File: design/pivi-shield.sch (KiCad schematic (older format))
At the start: 3 parts

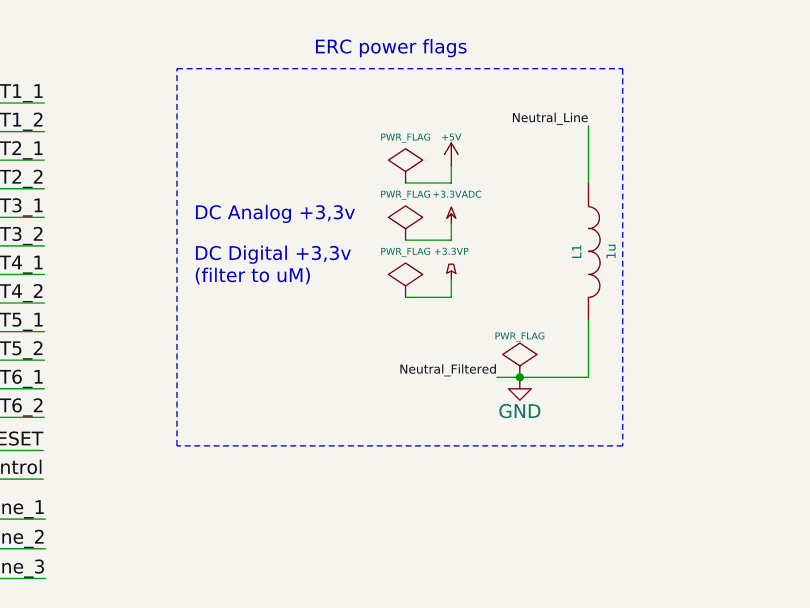
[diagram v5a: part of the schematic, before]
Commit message: Fix #10: main route not connected.
Right now we have the following power labels:
* +5V from 220v to Raspberry pi and voltage regulator.
* +3V3 from voltage regulator to microcontroller imput and measurement voltage circuit.
* +3.3VP DC digital +3.3v (filter to MCU).
* +3.3VADC DC analog +3.3v
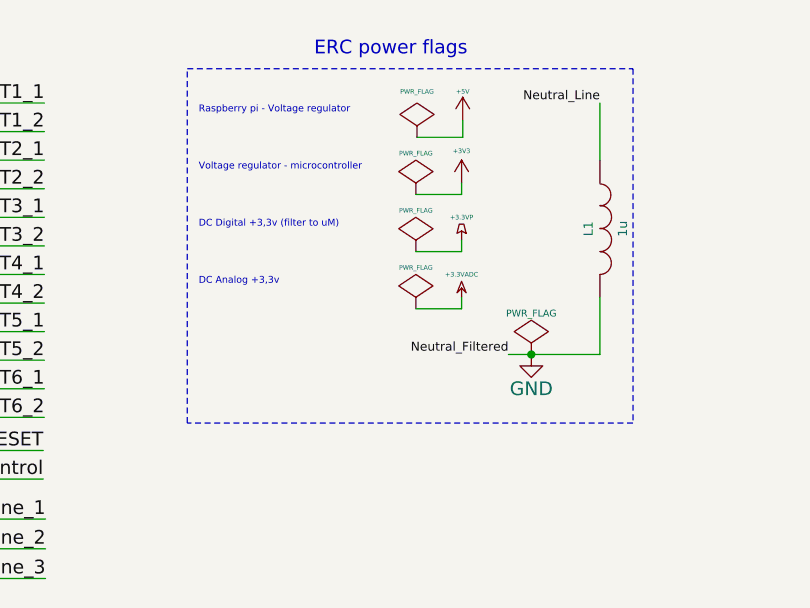
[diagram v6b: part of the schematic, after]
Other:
- note added: "DC Digital +3,3v (filter to uM)"
- note added: "Raspberry pi - Voltage regulator"
- note added: "Voltage regulator - microcontroller"
- note removed: "DC Digital +3,3v\n(filter to uM)"
- moved on the sheet: L1
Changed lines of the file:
@@
 LIBS:txs0104e
 LIBS:less
-LIBS:pivi-shield-cache
 EELAYER 25 0
 EELAYER END
@@
 L +5V #PWR01
 U 1 1 54928783
-P 5855 1475
-F 0 "#PWR01" H 5855 1565 20  0001 C CNN
-F 1 "+5V" H 5855 1600 30  0000 C CNN
-F 2 "" H 5855 1475 60  0000 C CNN
-F 3 "" H 5855 1475 60  0000 C CNN
-	1    5855 1475
+P 5905 1275
+F 0 "#PWR01" H 5905 1365 20  0001 C CNN
+F 1 "+5V" H 5905 1400 20  0000 C CNN
+F 2 "" H 5905 1275 60  0000 C CNN
+F 3 "" H 5905 1275 60  0000 C CNN
+	1    5905 1275
 	1    0    0    -1
 $EndComp
@@
 L PWR_FLAG #FLG02
 U 1 1 54928C31
-P 5655 1550
-F 0 "#FLG02" H 5655 1645 30  0001 C CNN
-F 1 "PWR_FLAG" H 5655 1750 30  0000 C CNN
-F 2 "" H 5655 1550 60  0000 C CNN
-F 3 "" H 5655 1550 60  0000 C CNN
-	1    5655 1550
+P 5705 1350
+F 0 "#FLG02" H 5705 1445 30  0001 C CNN
+F 1 "PWR_FLAG" H 5705 1550 20  0000 C CNN
+F 2 "" H 5705 1350 60  0000 C CNN
+F 3 "" H 5705 1350 60  0000 C CNN
+	1    5705 1350
 	1    0    0    -1
 $EndComp
@@
 F1 "pivi-power-supply.sch" 60
 $EndSheet
-$Comp
-L PWR_FLAG #FLG03
-U 1 1 548F827F
-P 5655 1800
-F 0 "#FLG03" H 5655 1895 30  0001 C CNN
-F 1 "PWR_FLAG" H 5655 2000 30  0000 C CNN
-F 2 "" H 5655 1800 60  0000 C CNN
-F 3 "" H 5655 1800 60  0000 C CNN
-	1    5655 1800
-	1    0    0    -1
-$EndComp
-$Comp
-L PWR_FLAG #FLG04
-U 1 1 548F891D
-P 5655 2050
-F 0 "#FLG04" H 5655 2145 30  0001 C CNN
-F 1 "PWR_FLAG" H 5655 2250 30  0000 C CNN
-F 2 "" H 5655 2050 60  0000 C CNN
-F 3 "" H 5655 2050 60  0000 C CNN
-	1    5655 2050
-	1    0    0    -1
-$EndComp
-$Comp
-L +3.3VADC #PWR05
-U 1 1 548F9301
-P 5855 1725
-F 0 "#PWR05" H 5855 1845 20  0001 C CNN
-F 1 "+3.3VADC" H 5880 1850 30  0000 C CNN
-F 2 "" H 5855 1725 60  0000 C CNN
-F 3 "" H 5855 1725 60  0000 C CNN
-	1    5855 1725
-	1    0    0    -1
-$EndComp
-$Comp
-L +3.3VP #PWR06
-U 1 1 548F9315
-P 5855 1975
-F 0 "#PWR06" H 5905 2005 20  0001 C CNN
-F 1 "+3.3VP" H 5855 2100 30  0000 C CNN
-F 2 "" H 5855 1975 60  0000 C CNN
-F 3 "" H 5855 1975 60  0000 C CNN
-	1    5855 1975
-	1    0    0    -1
-$EndComp
-Text Notes 4730 1725 0    60   ~ 0
-DC Analog +3,3v
-Text Notes 4730 2000 0    60   ~ 0
-DC Digital +3,3v\n(filter to uM)
+Text Notes 4750 1500 0    30   ~ 0
+Voltage regulator - microcontroller
+Text Notes 4750 1750 0    30   ~ 0
+DC Digital +3,3v (filter to uM)
 Text Label 1075 1450 0    60   ~ 0
 SDA1
@@
 TXD0
 $Comp
-L PWR_FLAG #FLG07
+L PWR_FLAG #FLG03
 U 1 1 5491BF45
-P 6155 2400
-F 0 "#FLG07" H 6155 2495 30  0001 C CNN
-F 1 "PWR_FLAG" H 6155 2580 30  0000 C CNN
-F 2 "" H 6155 2400 60  0000 C CNN
-F 3 "" H 6155 2400 60  0000 C CNN
-	1    6155 2400
+P 6205 2300
+F 0 "#FLG03" H 6205 2395 30  0001 C CNN
+F 1 "PWR_FLAG" H 6205 2480 30  0000 C CNN
+F 2 "" H 6205 2300 60  0000 C CNN
+F 3 "" H 6205 2300 60  0000 C CNN
+	1    6205 2300
 	1    0    0    -1
 $EndComp
@@
 NoConn ~ 3720 6330
 NoConn ~ 3720 6430
-Text Label 6055 2400 2    39   ~ 0
+Text Label 6105 2300 2    39   ~ 0
 Neutral_Filtered
 $Comp
 L INDUCTOR L1
 U 1 1 54C2A183
-P 6455 1850
-F 0 "L1" V 6405 1850 40  0000 C CNN
-F 1 "1u" V 6555 1850 40  0000 C CNN
-F 2 "Inductors_NEOSID:Neosid_Inductor_SM-NE30_SMD1210" V 6680 1850 60  0001 C CNN
-F 3 "" H 6455 1850 60  0000 C CNN
-	1    6455 1850
-	1    0    0    -1
-$EndComp
-$Comp
-L GND #PWR08
+P 6505 1750
+F 0 "L1" V 6455 1750 40  0000 C CNN
+F 1 "1u" V 6605 1750 40  0000 C CNN
+F 2 "Inductors_NEOSID:Neosid_Inductor_SM-NE30_SMD1210" V 6730 1750 60  0001 C CNN
+F 3 "" H 6505 1750 60  0000 C CNN
+	1    6505 1750
+	1    0    0    -1
+$EndComp
+$Comp
+L GND #PWR04
 U 1 1 54BFB838
-P 6155 2400
-F 0 "#PWR08" H 6155 2150 60  0001 C CNN
-F 1 "GND" H 6155 2250 60  0000 C CNN
-F 2 "" H 6155 2400 60  0000 C CNN
-F 3 "" H 6155 2400 60  0000 C CNN
-	1    6155 2400
-	1    0    0    -1
-$EndComp
-Text Label 6455 1300 2    39   ~ 0
+P 6205 2300
+F 0 "#PWR04" H 6205 2050 60  0001 C CNN
+F 1 "GND" H 6205 2150 60  0000 C CNN
+F 2 "" H 6205 2300 60  0000 C CNN
+F 3 "" H 6205 2300 60  0000 C CNN
+	1    6205 2300
+	1    0    0    -1
+$EndComp
+Text Label 6505 1200 2    39   ~ 0
 Neutral_Line
 Text Label 1100 5630 0    60   ~ 0
@@
 Current_AD_1
 $Comp
-L +3.3VADC #PWR09
+L +3.3VADC #PWR05
 U 1 1 55BC3462
 P 5680 4730
-F 0 "#PWR09" H 5830 4680 50  0001 C CNN
+F 0 "#PWR05" H 5830 4680 50  0001 C CNN
 F 1 "+3.3VADC" H 5680 4830 50  0000 C CNN
 F 2 "" H 5680 4730 60  0000 C CNN
@@
 $EndComp
 $Comp
-L GND #PWR010
+L GND #PWR06
 U 1 1 55BC74D1
 P 5680 5495
-F 0 "#PWR010" H 5680 5245 50  0001 C CNN
+F 0 "#PWR06" H 5680 5245 50  0001 C CNN
 F 1 "GND" H 5680 5345 50  0000 C CNN
 F 2 "" H 5680 5495 60  0000 C CNN
@@
 	1720 5530 1095 5530
 Wire Wire Line
-	5655 1550 5855 1550
-Wire Wire Line
-	5855 1550 5855 1475
-Wire Wire Line
-	5655 1800 5855 1800
-Wire Wire Line
-	5855 1800 5855 1725
-Wire Wire Line
-	5655 2050 5855 2050
-Wire Wire Line
-	5855 2050 5855 1975
+	5705 1350 5905 1350
+Wire Wire Line
+	5905 1350 5905 1275
 Wire Wire Line
 	3450 2075 4075 2075
@@
 Wire Wire Line
 	3450 1700 4075 1700
-Wire Notes Line
-	6605 1050 6605 2700
-Wire Notes Line
-	6605 2700 4655 2700
-Wire Notes Line
-	4655 2700 4655 1050
-Wire Notes Line
-	4655 1050 6605 1050
 Wire Wire Line
 	1320 6430 1720 6430
@@
 	1320 6330 1720 6330
 Wire Wire Line
-	6055 2400 6455 2400
-Wire Wire Line
-	6455 2400 6455 2150
-Wire Wire Line
-	6455 1550 6455 1300
-Connection ~ 6155 2400
+	6105 2300 6505 2300
+Wire Wire Line
+	6505 2300 6505 2050
+Wire Wire Line
+	6505 1450 6505 1200
+Connection ~ 6205 2300
 Wire Wire Line
 	1720 5630 1100 5630
@@
 Text Label 4080 3280 2    60   ~ 0
 Phase_Line_3
+Wire Notes Line
+	4700 1050 6650 1050
+Wire Notes Line
+	6650 2600 4700 2600
+Text Notes 4750 1250 0    30   ~ 0
+Raspberry pi - Voltage regulator
+Text Notes 4750 2000 0    30   ~ 0
+DC Analog +3,3v
+$Comp
+L PWR_FLAG #FLG07
+U 1 1 55F6DDEA
+P 5700 1600
+F 0 "#FLG07" H 5700 1695 50  0001 C CNN
+F 1 "PWR_FLAG" H 5700 1780 20  0000 C CNN
+F 2 "" H 5700 1600 60  0000 C CNN
+F 3 "" H 5700 1600 60  0000 C CNN
+	1    5700 1600
+	1    0    0    -1
+$EndComp
+Wire Wire Line
+	5700 1600 5900 1600
+$Comp
+L +3V3 #PWR08
+U 1 1 55F6E0D4
+P 5900 1550
+F 0 "#PWR08" H 5900 1400 50  0001 C CNN
+F 1 "+3V3" H 5900 1690 20  0000 C CNN
+F 2 "" H 5900 1550 60  0000 C CNN
+F 3 "" H 5900 1550 60  0000 C CNN
+	1    5900 1550
+	1    0    0    -1
+$EndComp
+Wire Wire Line
+	5900 1600 5900 1550
+$Comp
+L PWR_FLAG #FLG09
+U 1 1 55F70AB6
+P 5700 1850
+F 0 "#FLG09" H 5700 1945 50  0001 C CNN
+F 1 "PWR_FLAG" H 5700 2030 20  0000 C CNN
+F 2 "" H 5700 1850 60  0000 C CNN
+F 3 "" H 5700 1850 60  0000 C CNN
+	1    5700 1850
+	1    0    0    -1
+$EndComp
+Wire Wire Line
+	5700 1850 5900 1850
+Wire Wire Line
+	5900 1850 5900 1800
+$Comp
+L +3.3VP #PWR010
+U 1 1 55F70D1F
+P 5900 1800
+F 0 "#PWR010" H 6050 1750 50  0001 C CNN
+F 1 "+3.3VP" H 5900 1900 20  0000 C CNN
+F 2 "" H 5900 1800 60  0000 C CNN
+F 3 "" H 5900 1800 60  0000 C CNN
+	1    5900 1800
+	1    0    0    -1
+$EndComp
+$Comp
+L PWR_FLAG #FLG011
+U 1 1 55F71DAE
+P 5700 2100
+F 0 "#FLG011" H 5700 2195 50  0001 C CNN
+F 1 "PWR_FLAG" H 5700 2280 20  0000 C CNN
+F 2 "" H 5700 2100 60  0000 C CNN
+F 3 "" H 5700 2100 60  0000 C CNN
+	1    5700 2100
+	1    0    0    -1
+$EndComp
+Wire Wire Line
+	5700 2100 5900 2100
+Wire Wire Line
+	5900 2100 5900 2050
+$Comp
+L +3.3VADC #PWR012
+U 1 1 55F72017
+P 5900 2050
+F 0 "#PWR012" H 6050 2000 50  0001 C CNN
+F 1 "+3.3VADC" H 5900 2150 20  0000 C CNN
+F 2 "" H 5900 2050 60  0000 C CNN
+F 3 "" H 5900 2050 60  0000 C CNN
+	1    5900 2050
+	1    0    0    -1
+$EndComp
+Wire Notes Line
+	6650 1050 6650 2600
+Wire Notes Line
+	4700 2600 4700 1050
 $EndSCHEMATC
